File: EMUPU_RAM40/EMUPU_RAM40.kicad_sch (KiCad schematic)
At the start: 22 parts, among them J1 Conn_01x20_Socket, J2 Conn_01x20_Socket, J3 Barrel_Jack_Switch, J4 Conn_01x06_Pin, J5 Conn_01x08_Pin, SW1 SW_SPDT, SW2 SW_SPST, U1 PIC18F47Q43-IP, U2 628128

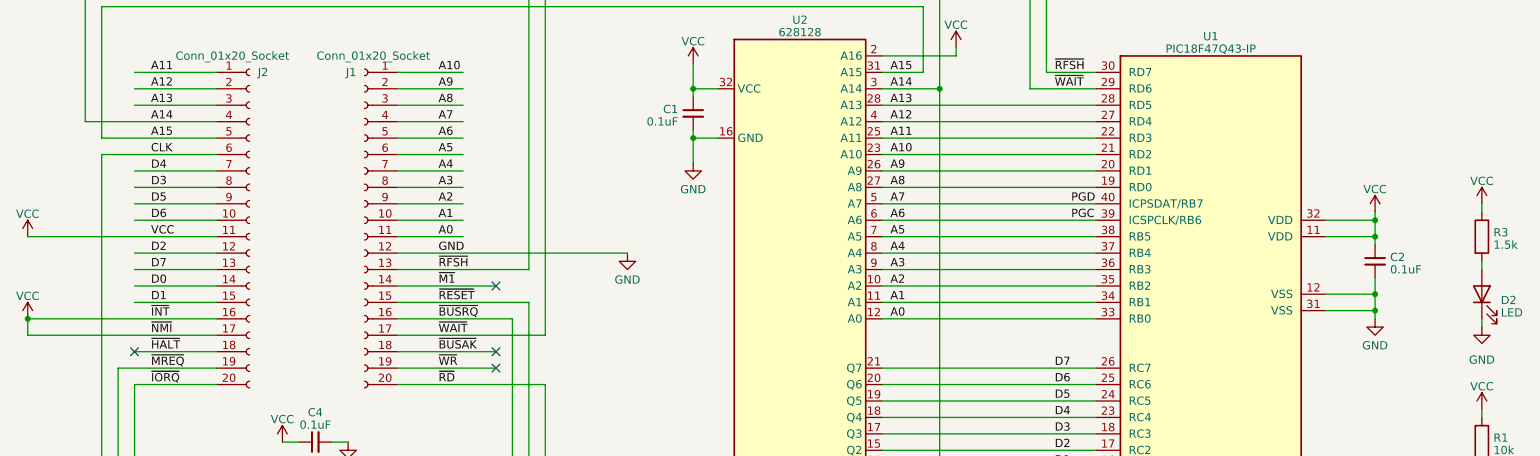
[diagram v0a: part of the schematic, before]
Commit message: 3rd before-freerouting, add Z80 pin-names, beta-border, and narrower board size and rearrangement of parts
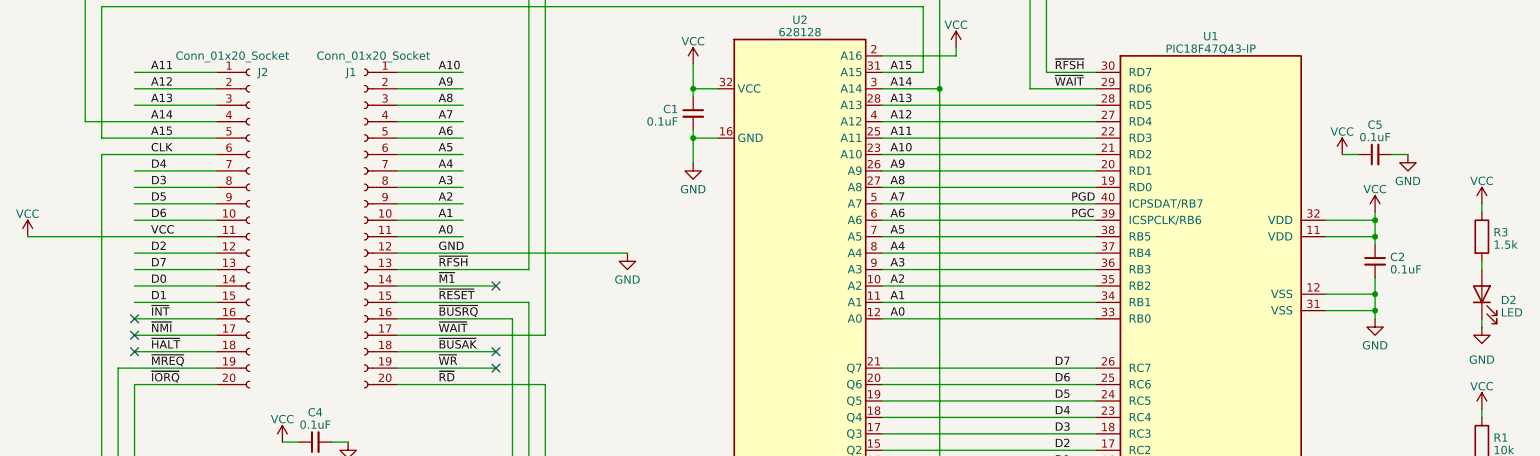
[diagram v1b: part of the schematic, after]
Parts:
- added C5: 0.1uF, Capacitor_THT:C_Disc_D3.0mm_W2.0mm_P2.50mm, symbol Device:C_Small
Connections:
- net GND: now also C5.2
- net VCC: now also C5.1; no longer J2.16 (Pin_16), J2.17 (Pin_17)
- new net ~{INT}: J2.16 (Pin_16)
- new net ~{NMI}: J2.17 (Pin_17)
- no-connect marks 11 -> 13
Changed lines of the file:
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@@
   (junction (at 255.27 36.83) (diameter 0) (color 0 0 0 0)
-  )
-  (junction (at 15.24 88.9) (diameter 0) (color 0 0 0 0)
   )
   (junction (at 223.52 76.2) (diameter 0) (color 0 0 0 0)
@@
   (no_connect (at 255.27 22.86))
   (no_connect (at 266.7 157.48))
+  (no_connect (at 31.75 91.44))
   (no_connect (at 87.63 83.82))
   (no_connect (at 31.75 93.98))
   (no_connect (at 262.89 111.76))
   (no_connect (at 87.63 93.98))
+  (no_connect (at 31.75 88.9))
   (no_connect (at 87.63 96.52))
   (wire (pts (xy 90.17 88.9) (xy 90.17 162.56))
@@
     (stroke (width 0) (type default))
   )
+  (wire (pts (xy 218.44 63.5) (xy 220.98 63.5))
+    (stroke (width 0) (type default))
+  )
   (wire (pts (xy 223.52 87.63) (xy 223.52 88.9))
     (stroke (width 0) (type default))
@@
     (stroke (width 0) (type default))
   )
-  (wire (pts (xy 15.24 88.9) (xy 44.45 88.9))
+  (wire (pts (xy 31.75 88.9) (xy 44.45 88.9))
     (stroke (width 0) (type default))
   )
@@
     (stroke (width 0) (type default))
   )
+  (wire (pts (xy 226.06 63.5) (xy 228.6 63.5))
+    (stroke (width 0) (type default))
+  )
   (wire (pts (xy 147.32 83.82) (xy 180.34 83.82))
     (stroke (width 0) (type default))
@@
     (stroke (width 0) (type default))
   )
-  (wire (pts (xy 15.24 88.9) (xy 15.24 91.44))
-    (stroke (width 0) (type default))
-  )
   (wire (pts (xy 147.32 58.42) (xy 180.34 58.42))
     (stroke (width 0) (type default))
@@
     (stroke (width 0) (type default))
   )
-  (wire (pts (xy 15.24 91.44) (xy 44.45 91.44))
-    (stroke (width 0) (type default))
-  )
   (wire (pts (xy 29.21 96.52) (xy 44.45 96.52))
     (stroke (width 0) (type default))
@@
   )
   (wire (pts (xy 215.9 73.66) (xy 223.52 73.66))
+    (stroke (width 0) (type default))
+  )
+  (wire (pts (xy 31.75 91.44) (xy 44.45 91.44))
     (stroke (width 0) (type default))
   )
@@
         (path "/e6d6b00c-3eac-46b2-864a-d30920c7bbcf"
           (reference "U2") (unit 1)
-        )
-      )
-    )
-  )
-  (symbol (lib_id "power:VCC") (at 15.24 88.9 0) (unit 1)
-    (in_bom yes) (on_board yes) (dnp no) (fields_autoplaced)
-    (property "Reference" "#PWR03" (at 15.24 92.71 0)
-      (effects (font (size 1.27 1.27)) hide)
-    )
-    (property "Value" "VCC" (at 15.24 85.3981 0)
-      (effects (font (size 1.27 1.27)))
-    )
-    (property "Footprint" "" (at 15.24 88.9 0)
-      (effects (font (size 1.27 1.27)) hide)
-    )
-    (property "Datasheet" "" (at 15.24 88.9 0)
-      (effects (font (size 1.27 1.27)) hide)
-    )
-    (pin "1")
-    (instances
-      (project "EMUPU_RAM"
-        (path "/6d2188b2-a6ec-4341-9e2f-19ddbe5554d2"
-          (reference "#PWR03") (unit 1)
-        )
-      )
-      (project "EMUPU_RAM40"
-        (path "/e6d6b00c-3eac-46b2-864a-d30920c7bbcf"
-          (reference "#PWR027") (unit 1)
         )
       )
@@
     )
   )
+  (symbol (lib_id "Device:C_Small") (at 223.52 63.5 90) (unit 1)
+    (in_bom yes) (on_board yes) (dnp no) (fields_autoplaced)
+    (property "Reference" "C5" (at 223.5263 58.928 90)
+      (effects (font (size 1.27 1.27)))
+    )
+    (property "Value" "0.1uF" (at 223.5263 60.849 90)
+      (effects (font (size 1.27 1.27)))
+    )
+    (property "Footprint" "Capacitor_THT:C_Disc_D3.0mm_W2.0mm_P2.50mm" (at 223.52 63.5 0)
+      (effects (font (size 1.27 1.27)) hide)
+    )
+    (property "Datasheet" "~" (at 223.52 63.5 0)
+      (effects (font (size 1.27 1.27)) hide)
+    )
+    (pin "1")
+    (pin "2")
+    (instances
+      (project "EMUPU_RAM"
+        (path "/6d2188b2-a6ec-4341-9e2f-19ddbe5554d2"
+          (reference "C5") (unit 1)
+        )
+      )
+      (project "EMUPU_RAM40"
+        (path "/e6d6b00c-3eac-46b2-864a-d30920c7bbcf"
+          (reference "C6") (unit 1)
+        )
+      )
+    )
+  )
   (symbol (lib_id "power:GND") (at 259.08 121.92 0) (unit 1)
     (in_bom yes) (on_board yes) (dnp no) (fields_autoplaced)
@@
         )
       )
+    )
+  )
+  (symbol (lib_id "power:VCC") (at 218.44 63.5 0) (unit 1)
+    (in_bom yes) (on_board yes) (dnp no) (fields_autoplaced)
+    (property "Reference" "#PWR025" (at 218.44 67.31 0)
+      (effects (font (size 1.27 1.27)) hide)
+    )
+    (property "Value" "VCC" (at 218.44 59.9981 0)
+      (effects (font (size 1.27 1.27)))
+    )
+    (property "Footprint" "" (at 218.44 63.5 0)
+      (effects (font (size 1.27 1.27)) hide)
+    )
+    (property "Datasheet" "" (at 218.44 63.5 0)
+      (effects (font (size 1.27 1.27)) hide)
+    )
+    (pin "1")
+    (instances
+      (project "EMUPU_RAM"
+        (path "/6d2188b2-a6ec-4341-9e2f-19ddbe5554d2"
+          (reference "#PWR025") (unit 1)
+        )
+      )
+      (project "EMUPU_RAM40"
+        (path "/e6d6b00c-3eac-46b2-864a-d30920c7bbcf"
+          (reference "#PWR021") (unit 1)
+        )
+      )
+    )
+  )
+  (symbol (lib_id "power:GND") (at 228.6 63.5 0) (unit 1)
+    (in_bom yes) (on_board yes) (dnp no) (fields_autoplaced)
+    (property "Reference" "#PWR026" (at 228.6 69.85 0)
+      (effects (font (size 1.27 1.27)) hide)
+    )
+    (property "Value" "GND" (at 228.6 67.6355 0)
+      (effects (font (size 1.27 1.27)))
+    )
+    (property "Footprint" "" (at 228.6 63.5 0)
+      (effects (font (size 1.27 1.27)) hide)
+    )
+    (property "Datasheet" "" (at 228.6 63.5 0)
+      (effects (font (size 1.27 1.27)) hide)
+    )
+    (pin "1")
+    (instances
+      (project "EMUPU_RAM"
+        (path "/6d2188b2-a6ec-4341-9e2f-19ddbe5554d2"
+          (reference "#PWR026") (unit 1)
+        )
+      )
+      (project "EMUPU_RAM40"
+        (path "/e6d6b00c-3eac-46b2-864a-d30920c7bbcf"
+          (reference "#PWR022") (unit 1)
+        )
+      )

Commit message: fix some on schematics
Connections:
- net GND: now also J4.6 (Pin_6); no longer J4.1 (Pin_1)
- net VCC: now also J4.4 (Pin_4); no longer J4.5 (Pin_5)
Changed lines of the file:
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@@
   (no_connect (at 266.7 154.94))
   (no_connect (at 261.62 30.48))
-  (no_connect (at 262.89 106.68))
+  (no_connect (at 266.7 119.38))
+  (no_connect (at 266.7 109.22))
   (no_connect (at 255.27 22.86))
   (no_connect (at 266.7 157.48))
@@
   (no_connect (at 87.63 83.82))
   (no_connect (at 31.75 93.98))
-  (no_connect (at 262.89 111.76))
   (no_connect (at 87.63 93.98))
   (no_connect (at 31.75 88.9))
@@
     (stroke (width 0) (type default))
   )
-  (wire (pts (xy 262.89 111.76) (xy 266.7 111.76))
+  (wire (pts (xy 259.08 111.76) (xy 266.7 111.76))
     (stroke (width 0) (type default))
   )
@@
     (stroke (width 0) (type default))
   )
-  (wire (pts (xy 259.08 121.92) (xy 259.08 119.38))
+  (wire (pts (xy 261.62 106.68) (xy 261.62 121.92))
     (stroke (width 0) (type default))
   )
@@
     (stroke (width 0) (type default))
   )
-  (wire (pts (xy 259.08 109.22) (xy 266.7 109.22))
-    (stroke (width 0) (type default))
-  )
   (wire (pts (xy 147.32 114.3) (xy 180.34 114.3))
     (stroke (width 0) (type default))
@@
     (stroke (width 0) (type default))
   )
-  (wire (pts (xy 259.08 107.95) (xy 259.08 109.22))
+  (wire (pts (xy 259.08 105.41) (xy 259.08 111.76))
     (stroke (width 0) (type default))
   )
@@
     (stroke (width 0) (type default))
   )
-  (wire (pts (xy 259.08 119.38) (xy 266.7 119.38))
-    (stroke (width 0) (type default))
-  )
   (wire (pts (xy 215.9 85.09) (xy 223.52 85.09))
     (stroke (width 0) (type default))
@@
     (stroke (width 0) (type default))
   )
-  (wire (pts (xy 262.89 106.68) (xy 266.7 106.68))
+  (wire (pts (xy 261.62 106.68) (xy 266.7 106.68))
     (stroke (width 0) (type default))
   )
@@
     )
   )
-  (symbol (lib_id "power:VCC") (at 259.08 107.95 0) (unit 1)
+  (symbol (lib_id "power:VCC") (at 259.08 105.41 0) (unit 1)
     (in_bom yes) (on_board yes) (dnp no)
-    (property "Reference" "#PWR09" (at 259.08 111.76 0)
-      (effects (font (size 1.27 1.27)) hide)
-    )
-    (property "Value" "VCC" (at 259.08 104.14 0)
-      (effects (font (size 1.27 1.27)))
-    )
-    (property "Footprint" "" (at 259.08 107.95 0)
-      (effects (font (size 1.27 1.27)) hide)
-    )
-    (property "Datasheet" "" (at 259.08 107.95 0)
+    (property "Reference" "#PWR09" (at 259.08 109.22 0)
+      (effects (font (size 1.27 1.27)) hide)
+    )
+    (property "Value" "VCC" (at 259.08 101.6 0)
+      (effects (font (size 1.27 1.27)))
+    )
+    (property "Footprint" "" (at 259.08 105.41 0)
+      (effects (font (size 1.27 1.27)) hide)
+    )
+    (property "Datasheet" "" (at 259.08 105.41 0)
       (effects (font (size 1.27 1.27)) hide)
     )
@@
     )
   )
-  (symbol (lib_id "power:GND") (at 259.08 121.92 0) (unit 1)
-    (in_bom yes) (on_board yes) (dnp no) (fields_autoplaced)
-    (property "Reference" "#PWR010" (at 259.08 128.27 0)
-      (effects (font (size 1.27 1.27)) hide)
-    )
-    (property "Value" "GND" (at 259.08 126.0555 0)
-      (effects (font (size 1.27 1.27)))
-    )
-    (property "Footprint" "" (at 259.08 121.92 0)
-      (effects (font (size 1.27 1.27)) hide)
-    )
-    (property "Datasheet" "" (at 259.08 121.92 0)
-      (effects (font (size 1.27 1.27)) hide)
-    )
+  (symbol (lib_id "power:GND") (at 261.62 121.92 0) (unit 1)
+    (in_bom yes) (on_board yes) (dnp no) (fields_autoplaced)
+    (property "Reference" "#PWR010" (at 261.62 128.27 0)
+      (effects (font (size 1.27 1.27)) hide)
+    )
+    (property "Value" "GND" (at 261.62 126.0555 0)
+      (effects (font (size 1.27 1.27)))
+    )
+    (property "Footprint" "" (at 261.62 121.92 0)
+      (effects (font (size 1.27 1.27)) hide)
+    )
+    (property "Datasheet" "" (at 261.62 121.92 0)
+      (effects (font (size 1.27 1.27)) hide)
+    )

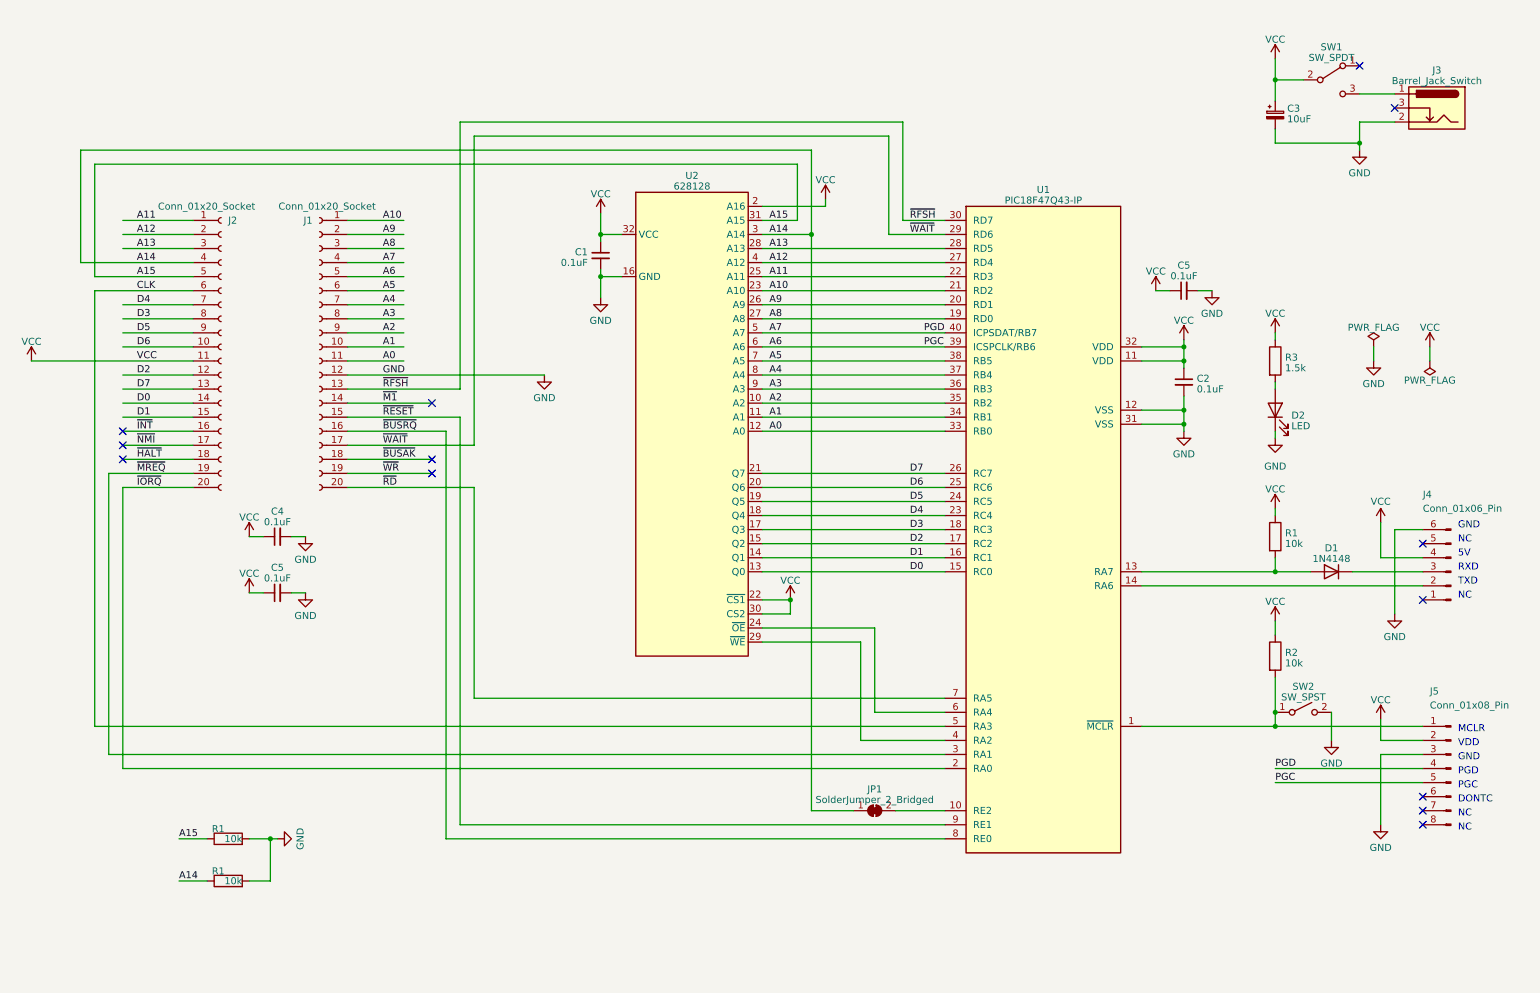
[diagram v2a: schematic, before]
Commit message: under construction for Rev003 done the follows * fix PowerPlug pin assignment * change /MREQ, /RD, /WR for full_direct * A jumper is assigned to SRAM CS2 (now pulled-up) * add jumpers on /MREQ, /RD, /WR * /INT, /M1 connection to RB5 and RA4. * cut a wire between PB5 and A13, * add pull-down resistors to A13 * add pull up resistors to /MREQ, /RD and /WR.
remains for the following
* add TEST pin
* add LEDs and resistors, including RESET, BUSACK, and HALT
* add pull down resistors to A15-A8, as needed.* add some jumpers for SDcard controls (A9-A12)
* add four jumpers for SDcard (A9-A12)

After confirming 8byte rewrite and reset bootloading, I will finishes the remains.
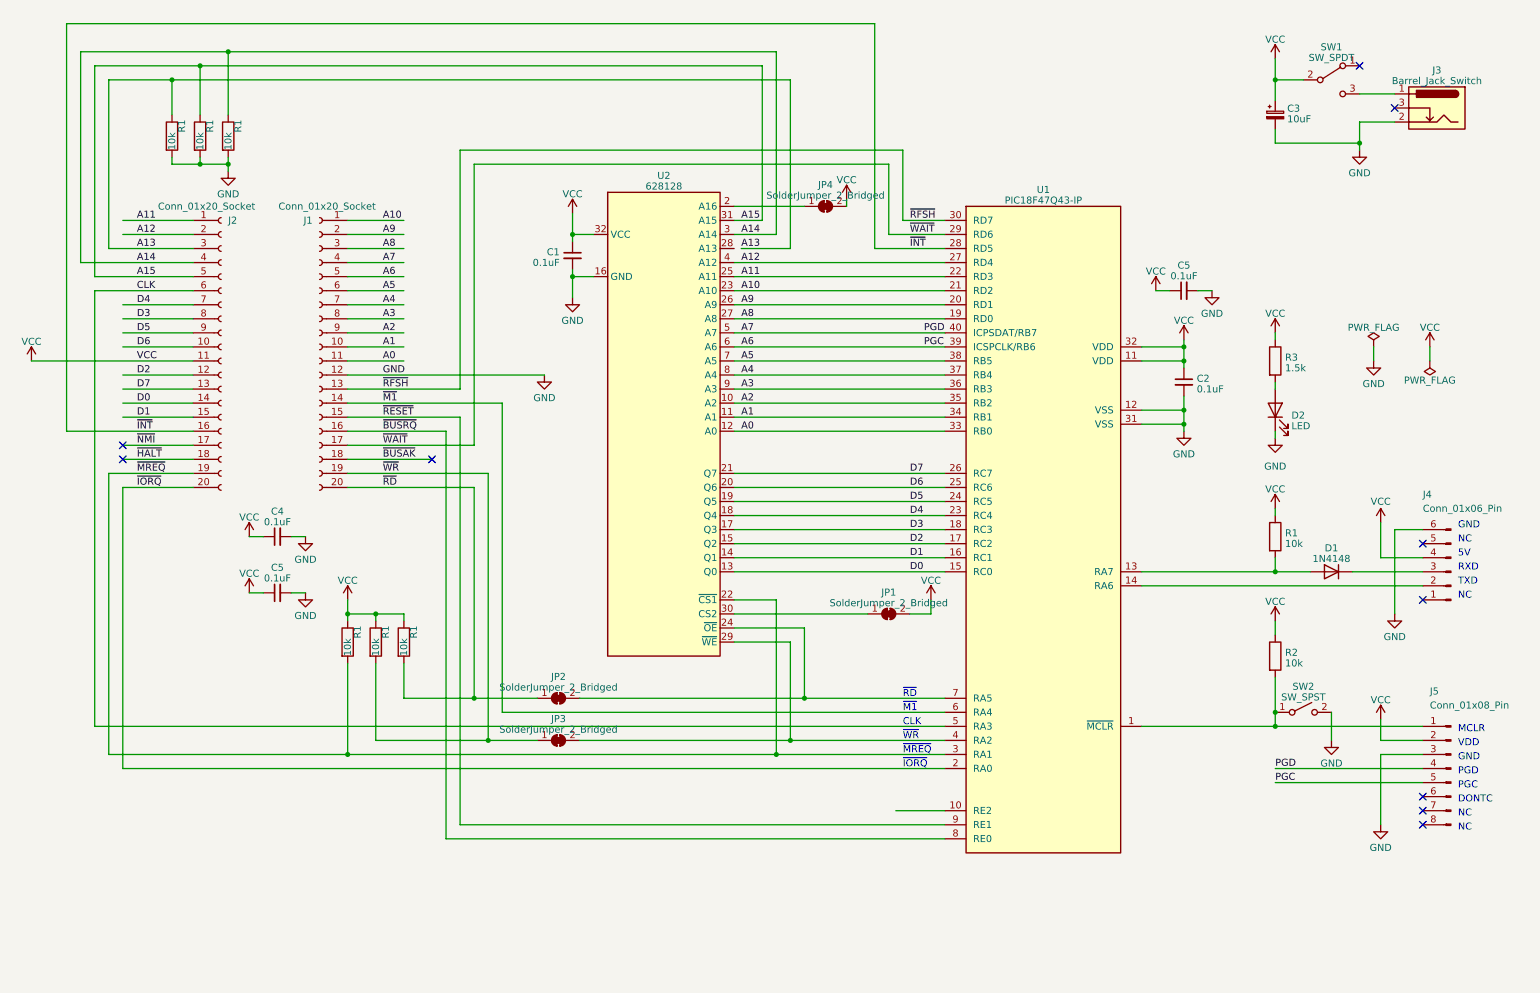
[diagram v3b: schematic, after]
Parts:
- added JP2, JP3, JP4: SolderJumper_2_Bridged, Jumper:SolderJumper-2_P1.3mm_Bridged_RoundedPad1.0x1.5mm, symbol Jumper:SolderJumper_2_Bridged
- added R1 (x4): 10k, Resistor_THT:R_Axial_DIN0204_L3.6mm_D1.6mm_P7.62mm_Horizontal, symbol Device:R
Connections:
- net A13: now also R1.1; no longer U1.28 (RD5), U2.28 (A13)
- net A14: now also R1.1; no longer JP1.1 (A), R1.1
- net A15: now also R1.1; no longer R1.1
- net GND: now also R1.2
- net VCC: now also JP1.2 (B), JP4.2 (B), R1.1, R1.1, R1.1; no longer U2.2 (A16), U2.22 (~{CS1}), U2.30 (CS2)
- net ~{INT}: now also U1.28 (RD5)
- net ~{M1}: now also U1.6 (RA4)
- net ~{MREQ}: now also U2.22 (~{CS1}), R1.2
- net ~{RD}: now also JP2.1 (A), R1.2; no longer U1.7 (RA5)
- net ~{WR}: now also JP3.1 (A), R1.2
- net at U2.24 (~{OE}): now also U1.7 (RA5), JP2.2 (B); no longer U1.6 (RA4)
- net at U1.4 (RA2), U2.29 (~{WE}): now also JP3.2 (B)
- net at U1.10 (RE2): no longer JP1.2 (B)
- new net: JP4.1 (A), U2.2 (A16)
- new net: JP1.1 (A), U2.30 (CS2)
- no-connect marks 13 -> 10
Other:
- note added: "CLK"
- note added: "~{IORQ}"
- note added: "~{M1}"
- note added: "~{MREQ}"
- note added: "~{RD}"
- note added: "~{WR}"
- title: (none) -> EMUPU_RAM40 Rev003 (full direct revision)
- moved on the sheet: C1, JP1, R1, U2
